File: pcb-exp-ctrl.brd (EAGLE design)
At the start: 100 x 80 mm, 5 parts, among them IC1 SAA1064, IC2 TINY13-20PU

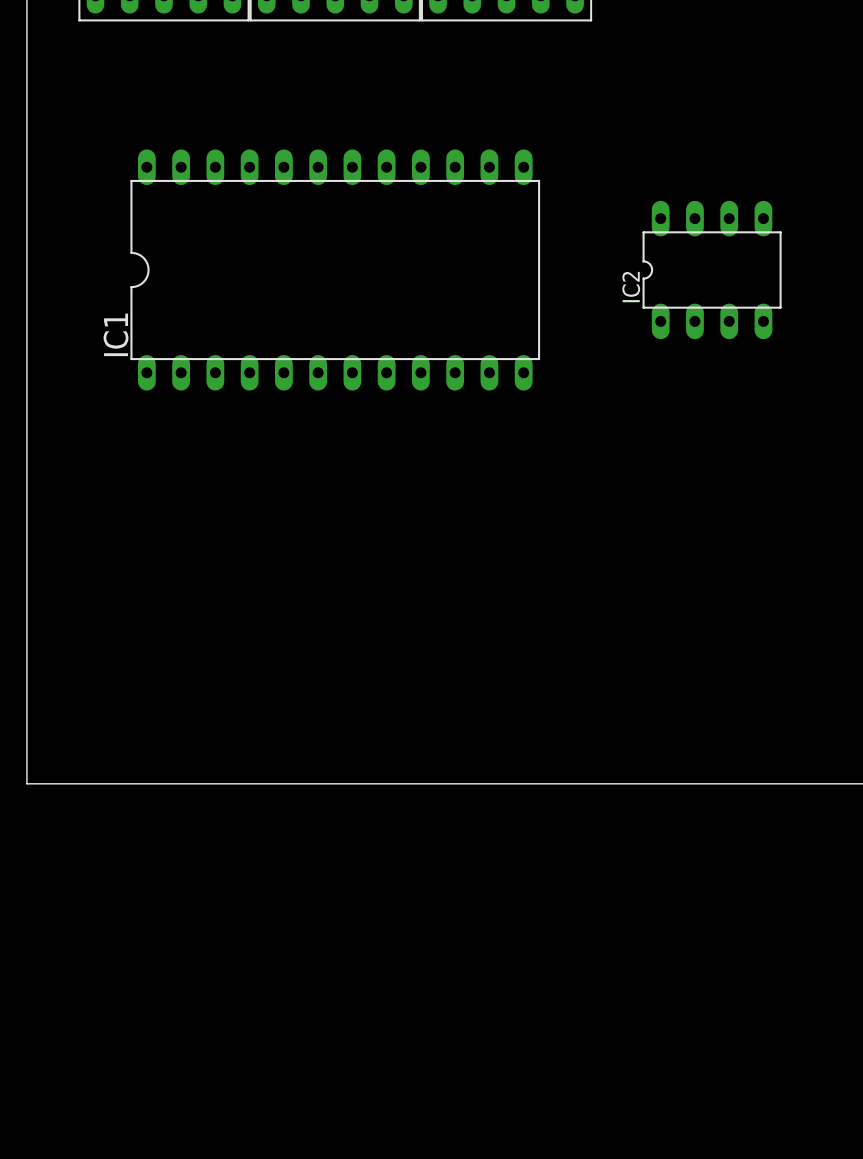
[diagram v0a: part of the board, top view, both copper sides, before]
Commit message: connect saa1064
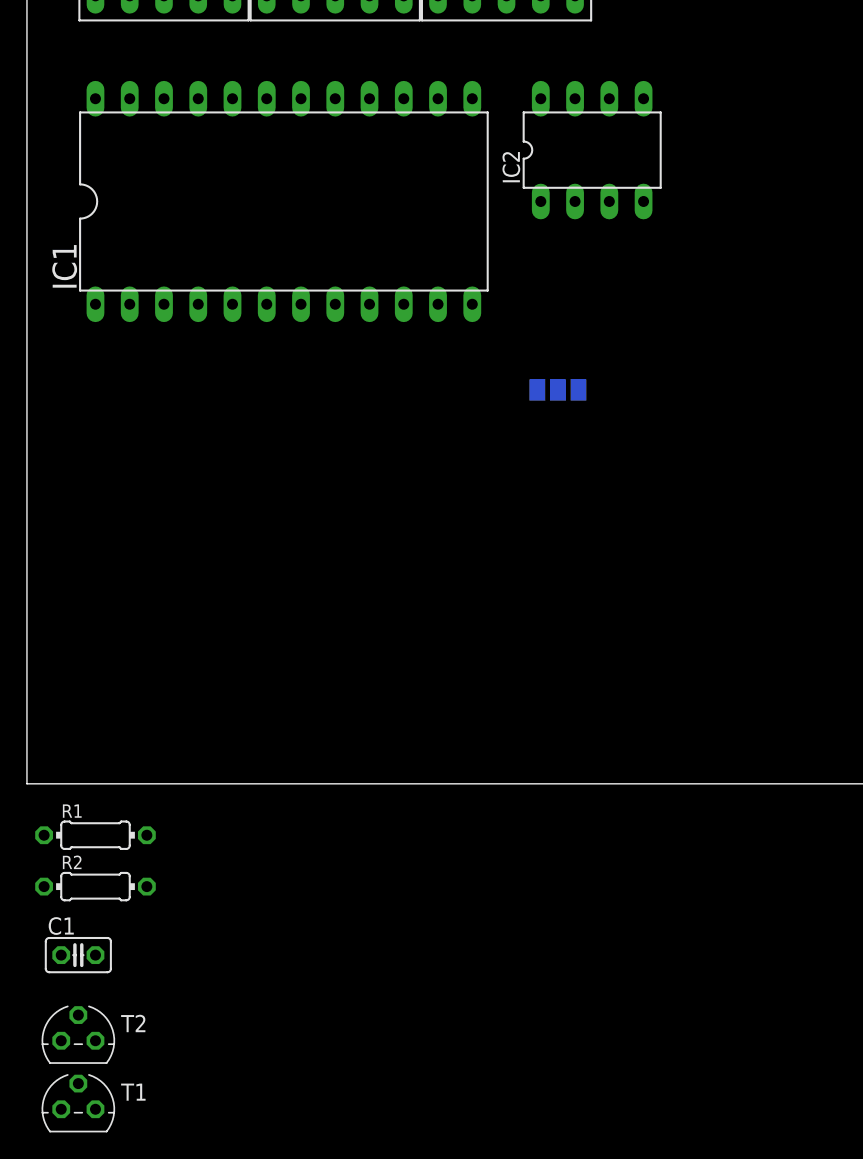
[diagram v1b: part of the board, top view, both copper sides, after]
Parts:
- added C1: 2.7n, rcl:C025-025X050
- added R1, R2: 10k, rcl:0204/7
- added SJ1: (no value), jumper:SJ_2
- added T1, T2: BC547, transistor:TO92
- moved IC2 12.6 mm to (41.9, 47.0)
- moved IC1 6.35 mm to (19.1, 43.2)
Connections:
- removed net VCC: IC1.13, IC2.8
- removed net VEE: IC1.12
- new net +5V: IC1.13, IC2.8, R1.2, R2.2, SJ1.3, T1.3, T2.3
- new net N$1: IC1.24, IC2.7, R2.1
- new net N$10: IC1.14, T2.2
- new net N$2: LED2.3, LED2.8, T2.1
- new net N$3: IC1.23, IC2.5, R1.1
- new net N$5: C1.1, IC1.2
- new net N$6: IC1.1, SJ1.2
- new net N$7: LED1.3, LED1.8, LED3.3, LED3.8, T1.1
- new net N$8: IC1.11, T1.2
- new net P1: IC1.10, LED1.7, LED2.7
- new net P10: IC1.16, LED3.6
- new net P11: IC1.17, LED3.4
- new net P12: IC1.18, LED3.2
- new net P13: IC1.19, LED3.1
- new net P14: IC1.20, LED3.9
- new net P15: IC1.21, LED3.10
- new net P16: IC1.22, LED3.5
- new net P2: IC1.9, LED1.6, LED2.6
- new net P3: IC1.8, LED1.4, LED2.4
- new net P4: IC1.7, LED1.2, LED2.2
- new net P5: IC1.6, LED1.1, LED2.1
- new net P6: IC1.5, LED1.9, LED2.9
- new net P7: IC1.4, LED1.10, LED2.10
- new net P8: IC1.3, LED1.5, LED2.5
- new net P9: IC1.15, LED3.7
- net GND: now also C1.2, IC1.12, SJ1.1

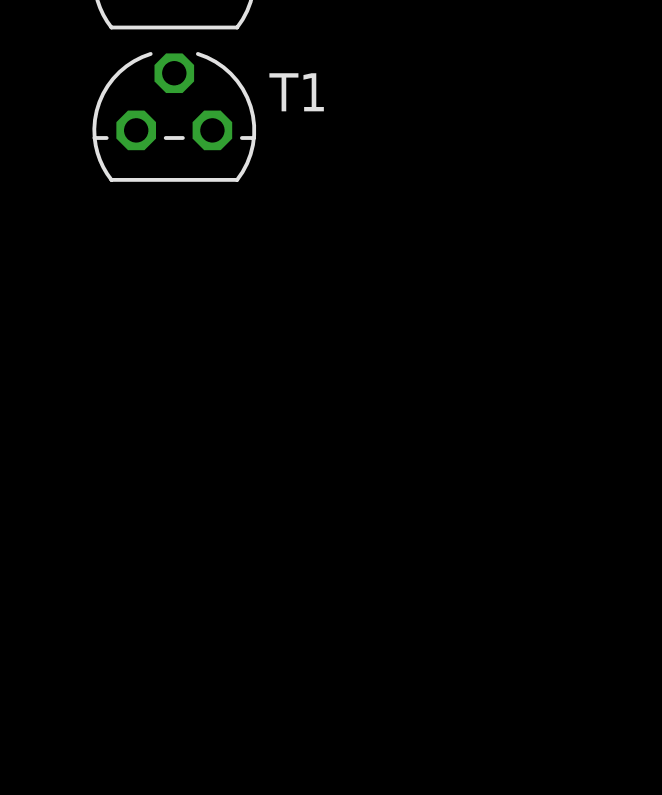
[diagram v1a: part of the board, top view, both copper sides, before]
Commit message: add 100n capacities for ICs
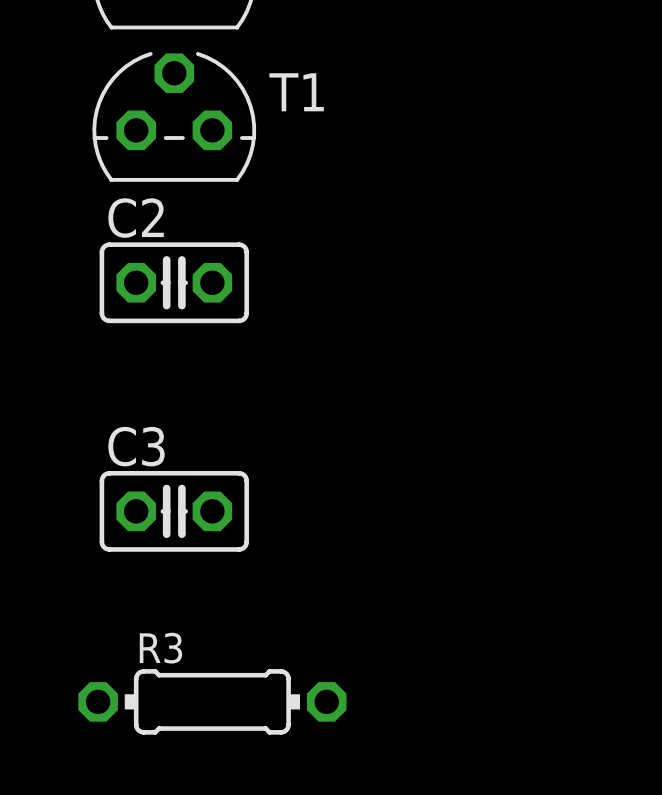
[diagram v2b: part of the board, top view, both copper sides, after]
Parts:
- added C2, C3: 100n, rcl:C025-025X050
- added R3: 10k, rcl:0204/7
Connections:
- new net N$11: IC2.1, R3.1
- net +5V: now also C2.1, C3.1, R3.2
- net GND: now also C2.2, C3.2
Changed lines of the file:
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@@
 <element name="T2" library="transistor" package="TO92" value="BC547" x="3.81" y="-19.05"/>
 <element name="T1" library="transistor" package="TO92" value="BC547" x="3.81" y="-24.13"/>
+<element name="C2" library="rcl" package="C025-025X050" value="100n" x="3.81" y="-29.21"/>
+<element name="C3" library="rcl" package="C025-025X050" value="100n" x="3.81" y="-36.83"/>
+<element name="R3" library="rcl" package="0204/7" value="10k" x="5.08" y="-43.18"/>
 </elements>
 <signals>
@@
 <contactref element="SJ1" pad="1"/>
 <contactref element="C1" pad="2"/>
+<contactref element="C2" pad="2"/>
+<contactref element="C3" pad="2"/>
 <wire x1="40.894" y1="29.21" x2="45.72" y2="43.18" width="0" layer="19" extent="16-16"/>
 <wire x1="33.02" y1="35.56" x2="40.894" y2="29.21" width="0" layer="19" extent="16-16"/>
 <wire x1="5.08" y1="-12.7" x2="40.894" y2="29.21" width="0" layer="19" extent="16-16"/>
+<wire x1="5.08" y1="-29.21" x2="5.08" y2="-12.7" width="0" layer="19" extent="1-1"/>
+<wire x1="5.08" y1="-36.83" x2="5.08" y2="-29.21" width="0" layer="19" extent="1-1"/>
 </signal>
 <signal name="P1">
@@
 </signal>
 <signal name="+5V">
-<contactref element="IC1" pad="13"/>
 <contactref element="IC2" pad="8"/>
-<contactref element="SJ1" pad="3"/>
+<contactref element="T2" pad="3"/>
+<contactref element="T1" pad="3"/>
+<contactref element="C2" pad="1"/>
 <contactref element="R1" pad="2"/>
 <contactref element="R2" pad="2"/>
-<contactref element="T2" pad="3"/>
-<contactref element="T1" pad="3"/>
+<contactref element="IC1" pad="13"/>
+<contactref element="SJ1" pad="3"/>
+<contactref element="C3" pad="1"/>
+<contactref element="R3" pad="2"/>
 <wire x1="33.02" y1="50.8" x2="38.1" y2="50.8" width="0" layer="19" extent="1-1"/>
 <wire x1="37.846" y1="29.21" x2="38.1" y2="50.8" width="0" layer="19" extent="16-16"/>
@@
 <wire x1="2.54" y1="-19.05" x2="8.89" y2="-7.62" width="0" layer="19" extent="1-1"/>
 <wire x1="2.54" y1="-24.13" x2="2.54" y2="-19.05" width="0" layer="19" extent="1-1"/>
+<wire x1="2.54" y1="-29.21" x2="2.54" y2="-24.13" width="0" layer="19" extent="1-1"/>
+<wire x1="2.54" y1="-36.83" x2="2.54" y2="-29.21" width="0" layer="19" extent="1-1"/>
+<wire x1="8.89" y1="-43.18" x2="2.54" y2="-36.83" width="0" layer="19" extent="1-1"/>
 </signal>
 <signal name="N$6">
@@
 <wire x1="3.81" y1="-17.145" x2="30.48" y2="50.8" width="0" layer="19" extent="1-1"/>
 </signal>
+<signal name="N$11">
+<contactref element="IC2" pad="1"/>
+<contactref element="R3" pad="1"/>
+<wire x1="1.27" y1="-43.18" x2="38.1" y2="43.18" width="0" layer="19" extent="1-1"/>
+</signal>
 </signals>

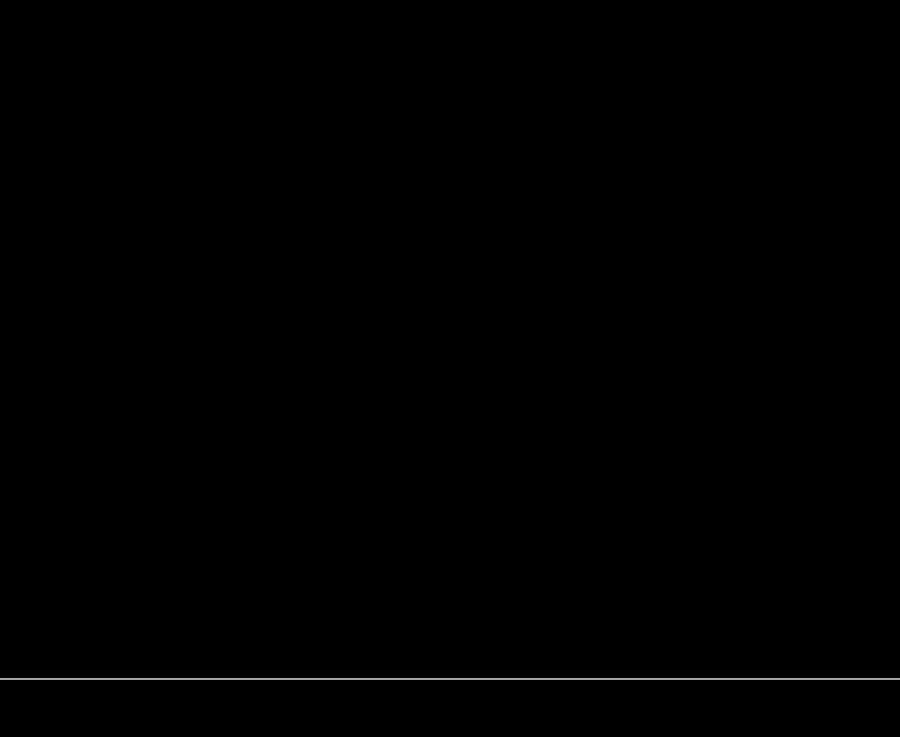
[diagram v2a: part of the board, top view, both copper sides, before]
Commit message: add programmer header and connect to uC
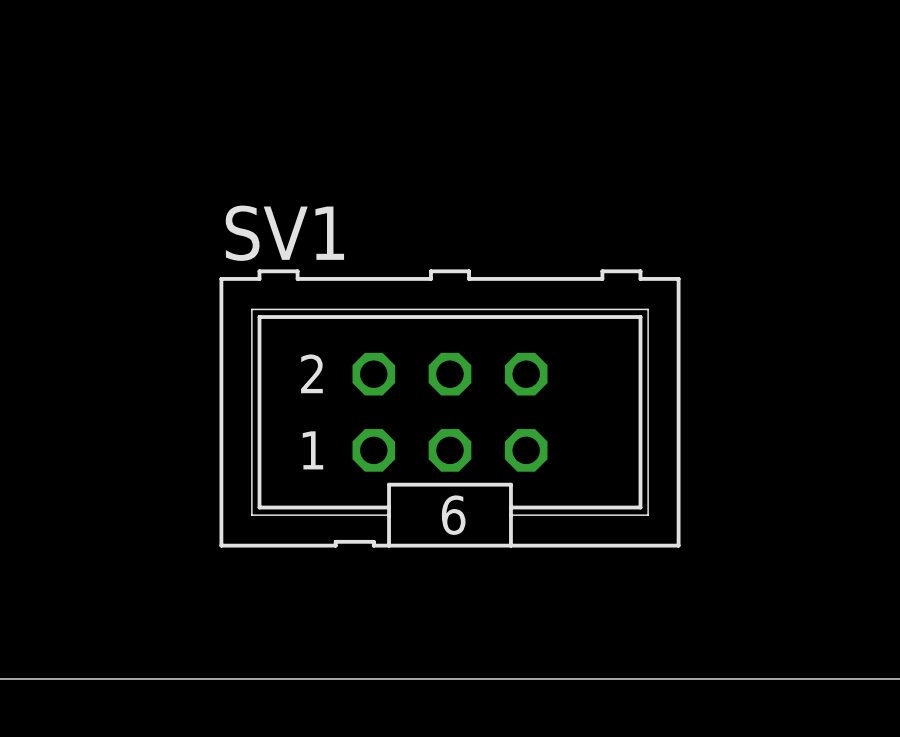
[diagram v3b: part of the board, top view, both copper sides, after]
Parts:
- added SV1: PROG, con-ml:ML6
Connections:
- removed net N$1: IC1.24, IC2.7, R2.1
- removed net N$11: IC2.1, R3.1
- removed net N$3: IC1.23, IC2.5, R1.1
- new net MISO: IC2.6, SV1.1
- new net MOSI: IC1.23, IC2.5, R1.1, SV1.4
- new net SCK: IC1.24, IC2.7, R2.1, SV1.3
- new net _RESET: IC2.1, R3.1, SV1.5
- net +5V: now also SV1.2
- net GND: now also SV1.6
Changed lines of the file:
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@@
 <element name="C3" library="rcl" package="C025-025X050" value="100n" x="3.81" y="-36.83"/>
 <element name="R3" library="rcl" package="0204/7" value="10k" x="5.08" y="-43.18"/>
+<element name="SV1" library="con-ml" package="ML6" value="PROG" x="40.64" y="8.89">
+<attribute name="OC_NEWARK" value="unknown" x="40.64" y="8.89" size="1.778" layer="27" display="off"/>
+<attribute name="MPN" value="" x="40.64" y="8.89" size="1.778" layer="27" display="off"/>
+<attribute name="MF" value="" x="40.64" y="8.89" size="1.778" layer="27" display="off"/>
+<attribute name="OC_FARNELL" value="unknown" x="40.64" y="8.89" size="1.778" layer="27" display="off"/>
+</element>
 </elements>
 <signals>
@@
 <contactref element="C2" pad="2"/>
 <contactref element="C3" pad="2"/>
+<contactref element="SV1" pad="6"/>
 <wire x1="40.894" y1="29.21" x2="45.72" y2="43.18" width="0" layer="19" extent="16-16"/>
 <wire x1="33.02" y1="35.56" x2="40.894" y2="29.21" width="0" layer="19" extent="16-16"/>
@@
 <wire x1="5.08" y1="-29.21" x2="5.08" y2="-12.7" width="0" layer="19" extent="1-1"/>
 <wire x1="5.08" y1="-36.83" x2="5.08" y2="-29.21" width="0" layer="19" extent="1-1"/>
+<wire x1="43.18" y1="10.16" x2="5.08" y2="-36.83" width="0" layer="19" extent="1-1"/>
 </signal>
 <signal name="P1">
@@
 <wire x1="5.08" y1="-19.05" x2="22.86" y2="58.42" width="0" layer="19" extent="1-1"/>
 </signal>
-<signal name="N$1">
+<signal name="SCK">
 <contactref element="IC2" pad="7"/>
 <contactref element="IC1" pad="24"/>
 <contactref element="R2" pad="1"/>
+<contactref element="SV1" pad="3"/>
 <wire x1="5.08" y1="50.8" x2="40.64" y2="50.8" width="0" layer="19" extent="1-1"/>
 <wire x1="1.27" y1="-7.62" x2="5.08" y2="50.8" width="0" layer="19" extent="1-1"/>
-</signal>
-<signal name="N$3">
+<wire x1="40.64" y1="7.62" x2="1.27" y2="-7.62" width="0" layer="19" extent="1-1"/>
+</signal>
+<signal name="MOSI">
 <contactref element="IC2" pad="5"/>
 <contactref element="IC1" pad="23"/>
 <contactref element="R1" pad="1"/>
+<contactref element="SV1" pad="4"/>
 <wire x1="7.62" y1="50.8" x2="45.72" y2="50.8" width="0" layer="19" extent="1-1"/>
 <wire x1="1.27" y1="-3.81" x2="7.62" y2="50.8" width="0" layer="19" extent="1-1"/>
+<wire x1="40.64" y1="10.16" x2="1.27" y2="-3.81" width="0" layer="19" extent="1-1"/>
 </signal>
 <signal name="+5V">
@@
 <contactref element="C3" pad="1"/>
 <contactref element="R3" pad="2"/>
+<contactref element="SV1" pad="2"/>
 <wire x1="33.02" y1="50.8" x2="38.1" y2="50.8" width="0" layer="19" extent="1-1"/>
 <wire x1="37.846" y1="29.21" x2="38.1" y2="50.8" width="0" layer="19" extent="16-16"/>
@@
 <wire x1="2.54" y1="-36.83" x2="2.54" y2="-29.21" width="0" layer="19" extent="1-1"/>
 <wire x1="8.89" y1="-43.18" x2="2.54" y2="-36.83" width="0" layer="19" extent="1-1"/>
+<wire x1="38.1" y1="10.16" x2="8.89" y2="-43.18" width="0" layer="19" extent="1-1"/>
 </signal>
 <signal name="N$6">
@@
 <wire x1="3.81" y1="-17.145" x2="30.48" y2="50.8" width="0" layer="19" extent="1-1"/>
 </signal>
-<signal name="N$11">
+<signal name="_RESET">
 <contactref element="IC2" pad="1"/>
 <contactref element="R3" pad="1"/>
+<contactref element="SV1" pad="5"/>
 <wire x1="1.27" y1="-43.18" x2="38.1" y2="43.18" width="0" layer="19" extent="1-1"/>
+<wire x1="43.18" y1="7.62" x2="1.27" y2="-43.18" width="0" layer="19" extent="1-1"/>
+</signal>
+<signal name="MISO">
+<contactref element="IC2" pad="6"/>
+<contactref element="SV1" pad="1"/>
+<wire x1="38.1" y1="7.62" x2="43.18" y2="50.8" width="0" layer="19" extent="1-1"/>
 </signal>
 </signals>
